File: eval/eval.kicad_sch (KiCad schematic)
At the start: 0 parts

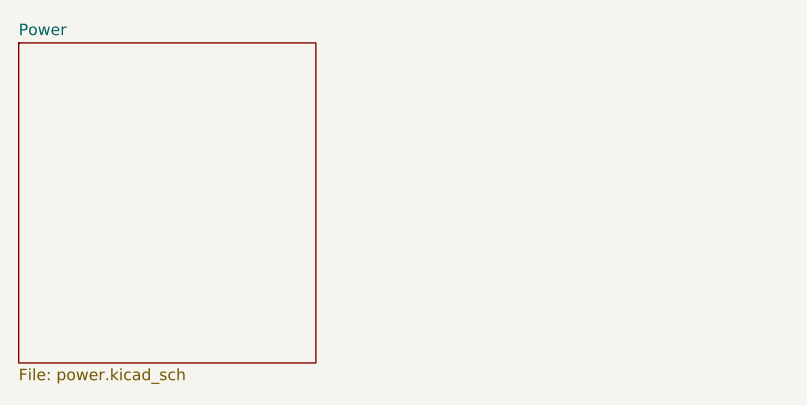
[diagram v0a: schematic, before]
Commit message: new eval imus
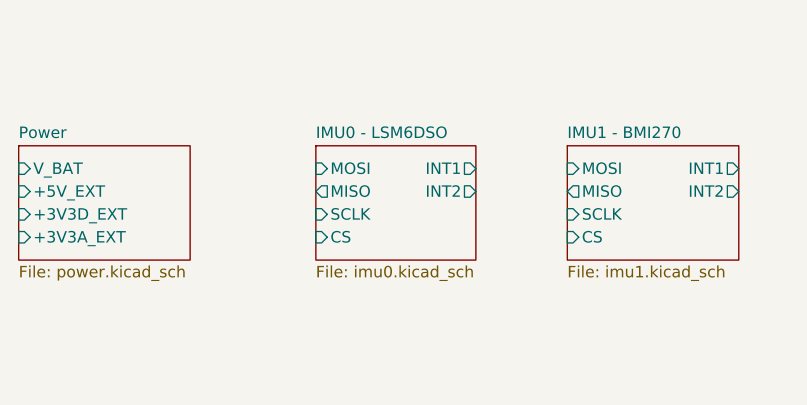
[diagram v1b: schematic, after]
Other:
- added sheet IMU0 - LSM6DSO (imu0.kicad_sch)
- added sheet IMU1 - BMI270 (imu1.kicad_sch)
- sheet Power ports: added +3V3A_EXT, +3V3D_EXT, +5V_EXT, V_BAT; removed none

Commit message: eval sd card usb
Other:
- added sheet Baro - BMP388 (baro.kicad_sch)
- added sheet Mag - QMC5883P (mag.kicad_sch)
- added sheet SD Card (sdcard.kicad_sch)
- added sheet USB (usb.kicad_sch)

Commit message: mcu
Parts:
- added J6: SWD, Connector_PinHeader_2.54mm:PinHeader_1x05_P2.54mm_Vertical, symbol Connector:Conn_01x05_Pin
- added J7: 5V_CONN, symbol Connector:Conn_01x03_Pin
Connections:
- net USB/+5V_USB: now also J7.1 (Pin_1)
- new net +3V3D: J6.1 (Pin_1)
- new net GND: J6.3 (Pin_3)
- new net MCU - STM32F405RG/NRST: J6.5 (Pin_5)
- new net MCU - STM32F405RG/SWCLK: J6.2 (Pin_2)
- new net MCU - STM32F405RG/SWDIO: J6.4 (Pin_4)
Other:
- added sheet MCU - STM32F405RG (mcu.kicad_sch)
